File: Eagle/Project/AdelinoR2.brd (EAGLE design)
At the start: 47 x 53.3 mm, 79 parts, among them J1 DC-044-A, J2 YELLOW-8P-2.54, J3 YELLOW-6P-2.54, J4 YELLOW-8P-2.54, J5 YELLOW-8P-2.54, J6 4P-2.0, J7 YELLOW-2X3P-2.54, J8 4P-2.0, Q1 NCE3407A, Q2 CJ2305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

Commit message: Routing wip.
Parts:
- removed D1, D2: 1K 1/10W, Seeed-Fuse:D0603
- added ESD1: PRTR5V0U2X, Seeed-OPL-2017-01-Diode-james:SOT-143B
- moved Q2 17.5 mm to (7.49, 26.7), turned to 90 degrees
- moved R8 14.4 mm to (7.49, 28.8), turned to 270 degrees
- moved F1 8.42 mm to (8.51, 39.0), turned to 0 degrees
- moved R2 3.67 mm to (11.3, 36.4), turned to 0 degrees
- moved R3 3.64 mm to (11.3, 34.0), turned to 0 degrees
- moved D6 1.09 mm to (5.84, 22.2)
- moved L1 1.08 mm to (8.51, 34.0)
- moved C1 0.13 mm to (18.4, 26.7)
- moved C10 0.13 mm to (14.6, 26.7)
- moved C9 0.13 mm to (16.8, 26.7)
- moved R13 0.13 mm to (37.1, 24.9)
- moved R14 0.13 mm to (34.9, 24.9)
- moved R6 0.13 mm to (11.9, 27.6)
- moved X1 0.13 mm to (33.0, 45.8)
- moved R7 0.13 mm to (11.9, 25.8)
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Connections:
- net GND: no longer D1.1, D2.1
- net N$1: now also ESD1.3; no longer D1.2
- net N$2: now also ESD1.2; no longer D2.2
- net N$9: now also ESD1.4
- net UGND: now also ESD1.1
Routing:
- net RESET: track 21.1 -> 110.1 mm
- net PIN_D13: track 2.95 -> 88.8 mm, vias 0 -> 3
- net ACT_LED: track 0.00 -> 43.7 mm, vias 0 -> 4
- net PIN_D11: track 3.07 -> 37.6 mm, vias 0 -> 2
- net PIN_D10: track 2.70 -> 32.9 mm, vias 0 -> 1
- net PIN_D12: track 2.70 -> 30.6 mm, vias 0 -> 1
- net PIN_D9: track 2.57 -> 29.1 mm, vias 0 -> 1
- net PIN_D8: track 2.45 -> 26.0 mm, vias 0 -> 1
- net VUSB: track 19.3 -> 41.0 mm, vias 0 -> 1
- net PIN_D5: track 2.82 -> 24.1 mm, vias 0 -> 1
- net PIN_D6: track 2.57 -> 21.0 mm, vias 0 -> 1
- net PIN_D4: track 2.82 -> 20.4 mm, vias 0 -> 1
- net +3V3: track 26.1 -> 43.2 mm
- net PIN_D3: track 63.7 -> 49.7 mm
- net N$9: track 17.7 -> 4.82 mm
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- added copper zone on layer 16, net +5V

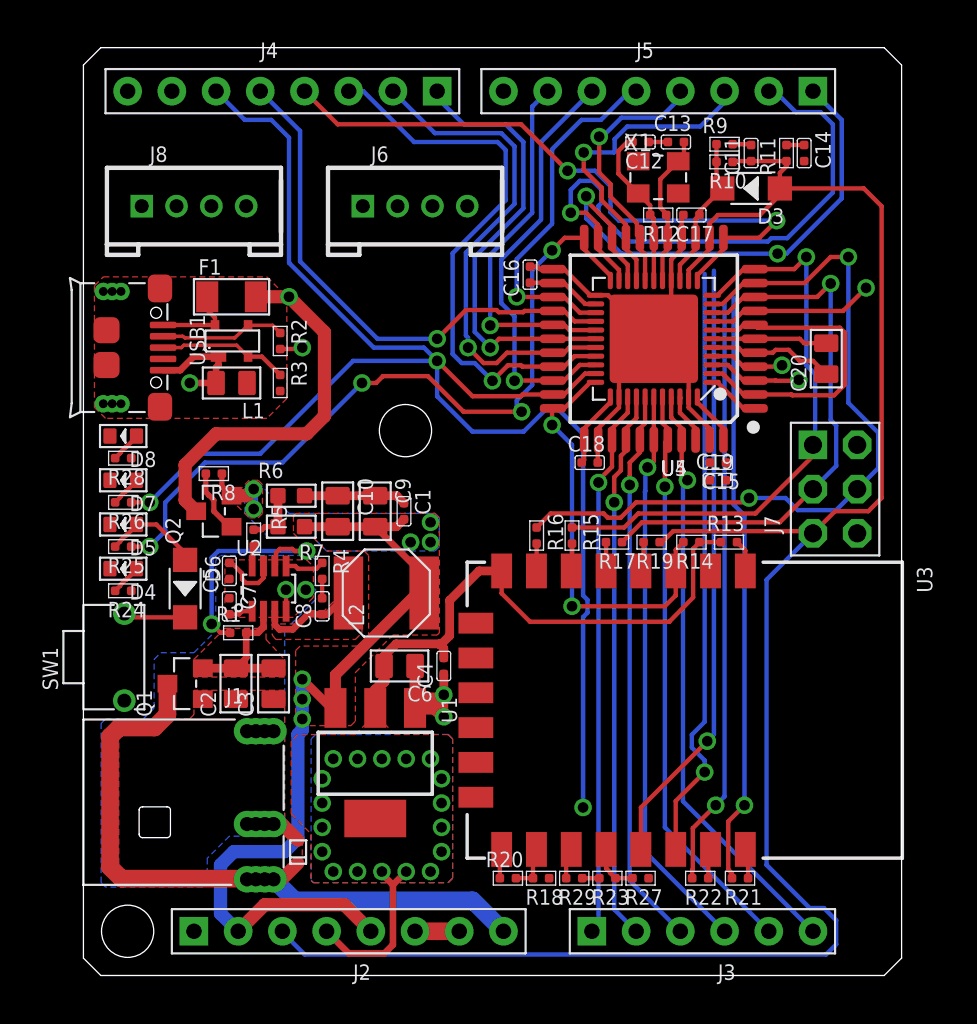
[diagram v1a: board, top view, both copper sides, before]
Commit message: Add ATECC608 crypto chip; routing wip.
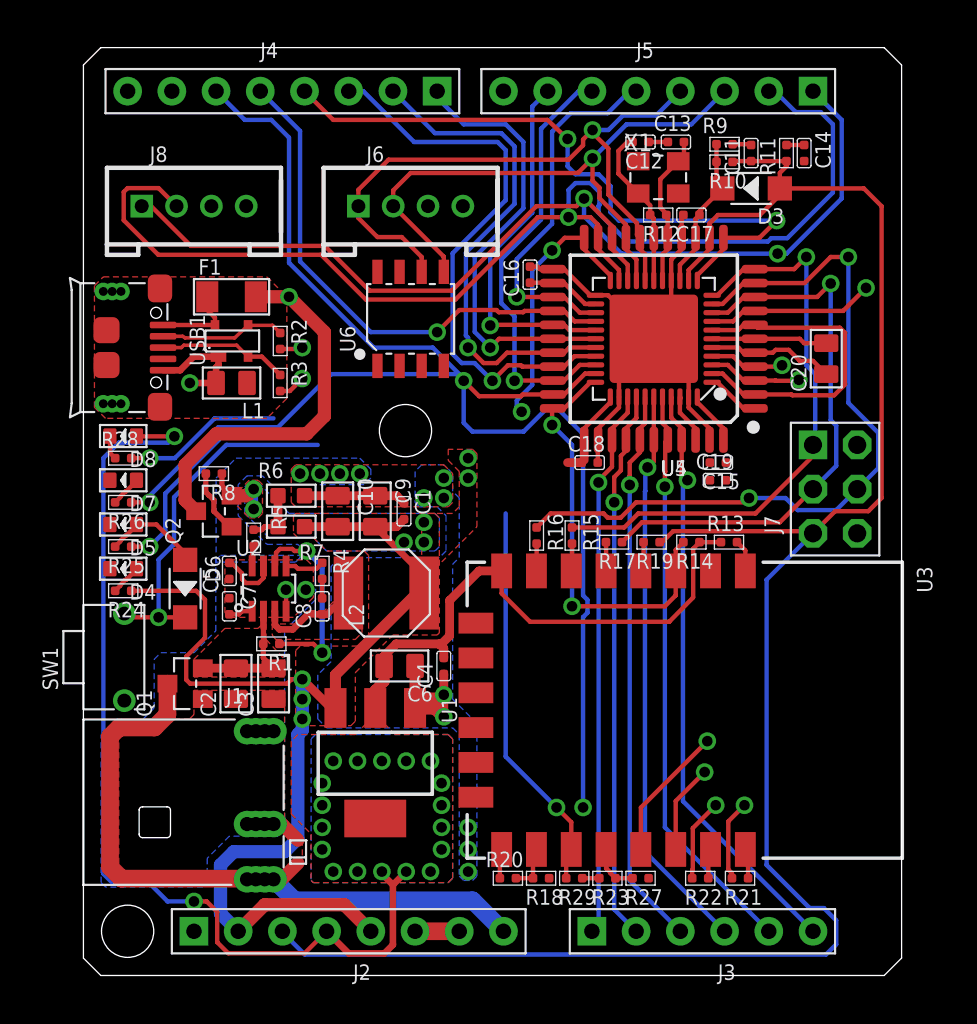
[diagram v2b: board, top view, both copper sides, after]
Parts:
- added U6: ATECC608-SOIC8, Adelino-Misc:SOIC8-1.27-5X4MM
- moved R1 2.01 mm to (10.8, 19.1), turned to 270 degrees
- moved J6 0.25 mm to (18.8, 44.2)
- turned R28 to 90 degrees
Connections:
- removed net PIN_D2: J5.3, J6.2, U3.19, U4.19, U5.19
- removed net PIN_D3: J5.4, J6.1, U3.20, U4.18, U5.18
- removed net _ESP: D8.+, R28.2
- new net N$4: D8.-, R28.1
- new net PIN_D2_SDA: J5.3, J6.2, U3.19, U4.19, U5.19, U6.5
- new net PIN_D3_SCL: J5.4, J6.1, U3.20, U4.18, U5.18, U6.6
- net +3V3: now also D8.+; no longer R28.1
- net +5V: now also U6.8
- net GND: now also U6.4
- net GPIO2_LED: now also R28.2; no longer D8.-
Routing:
- net PIN_D2: track 53.9 -> 0.00 mm, vias 2 -> 0
- net PIN_D3: track 49.7 -> 0.00 mm, vias 2 -> 0
- net +3V3: track 43.2 -> 90.1 mm, vias 18 -> 20
- net PIN_D2_SDA: track 0.00 -> 43.1 mm, vias 0 -> 2
- net PIN_D3_SCL: track 0.00 -> 43.1 mm, vias 0 -> 2
- net GPIO2_LED: track 1.77 -> 31.8 mm, vias 0 -> 2
- net +5V: track 74.9 -> 92.1 mm, vias 8 -> 10
- net RSTAT: track 4.66 -> 21.4 mm, vias 0 -> 1
- net ACT_LED: track 43.7 -> 29.2 mm, vias 4 -> 3
- net PIN_D1: track 68.0 -> 73.5 mm
- net SW_EN: track 13.4 -> 11.6 mm
- net _ESP: track 1.80 -> 0.00 mm
- net D+: track 4.30 -> 5.86 mm, vias 1 -> 2
- net N$4: track 0.00 -> 1.39 mm
- net PIN_D11: track 37.6 -> 38.5 mm
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
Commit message: Routing wip.
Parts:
- moved R27 2.16 mm to (29.8, 5.59), turned to 90 degrees
- moved R3 1.94 mm to (11.7, 35.9), turned to 90 degrees
- moved R23 1.65 mm to (31.8, 5.59), turned to 90 degrees
- moved R10 0.64 mm to (37.5, 46.7)
- moved R9 0.64 mm to (37.5, 47.8)
- moved R18 0.64 mm to (25.7, 5.59)
- moved R20 0.64 mm to (23.7, 5.59)
- moved R2 0.64 mm to (11.7, 37.0), turned to 90 degrees
- moved C11 0.63 mm to (39.0, 47.2)
- moved C14 0.63 mm to (42.0, 47.2)
- moved D3 0.63 mm to (39.0, 45.2)
- moved R11 0.63 mm to (41.0, 47.2)
- moved C20 0.52 mm to (42.8, 35.9)
- moved R15 0.38 mm to (28.1, 24.9), turned to 270 degrees
- moved R16 0.38 mm to (26.0, 24.9), turned to 270 degrees
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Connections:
- net +3V3: now also R28.1; no longer D8.+
- net GPIO2_LED: now also D8.-; no longer R28.2
- net N$4: now also D8.+, R28.2; no longer D8.-, R28.1
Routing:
- net +5V: track 92.1 -> 219.5 mm, vias 10 -> 13
- net PIN_D1: track 73.5 -> 140.7 mm, vias 2 -> 4
- net PIN_D0: track 64.9 -> 126.3 mm, vias 3 -> 4
- net RSTAT: track 21.4 -> 81.4 mm, vias 1 -> 2
- net AT_SS: track 9.64 -> 64.0 mm, vias 1 -> 3
- net UGND: track 13.9 -> 54.6 mm, vias 1 -> 2
- net D+: track 5.86 -> 42.2 mm
- net PIN_D3_SCL: track 43.1 -> 78.0 mm, vias 2 -> 3
- net PIN_D7: track 3.07 -> 37.7 mm, vias 0 -> 2
- net D-: track 6.68 -> 41.0 mm
- net PIN_D2_SDA: track 43.1 -> 73.1 mm, vias 2 -> 3
- net VUSB: track 41.0 -> 70.8 mm, vias 1 -> 3
- net +3V3: track 90.1 -> 109.9 mm
- net GPIO2_LED: track 31.8 -> 51.4 mm
- net ACT_LED: track 29.2 -> 45.2 mm, vias 3 -> 2
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
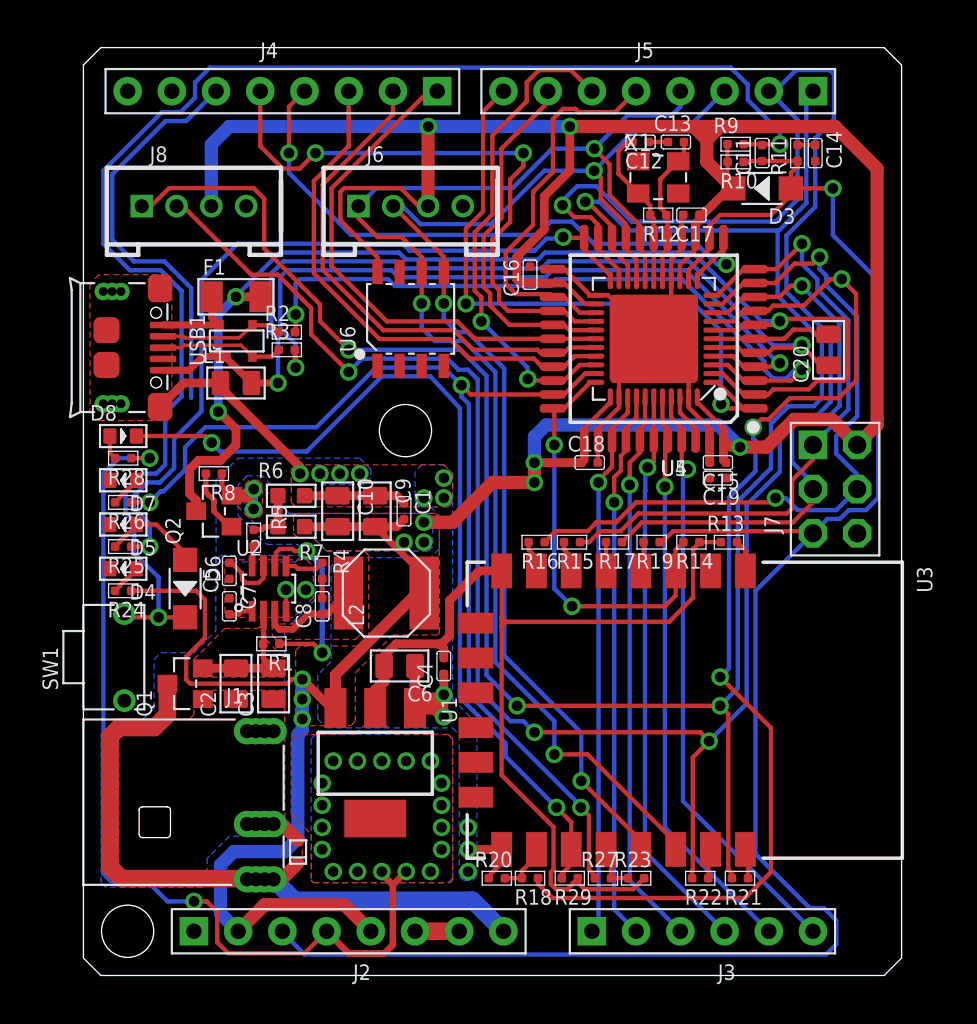
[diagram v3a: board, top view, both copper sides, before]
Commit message: Add decoupling cap for ECC608.
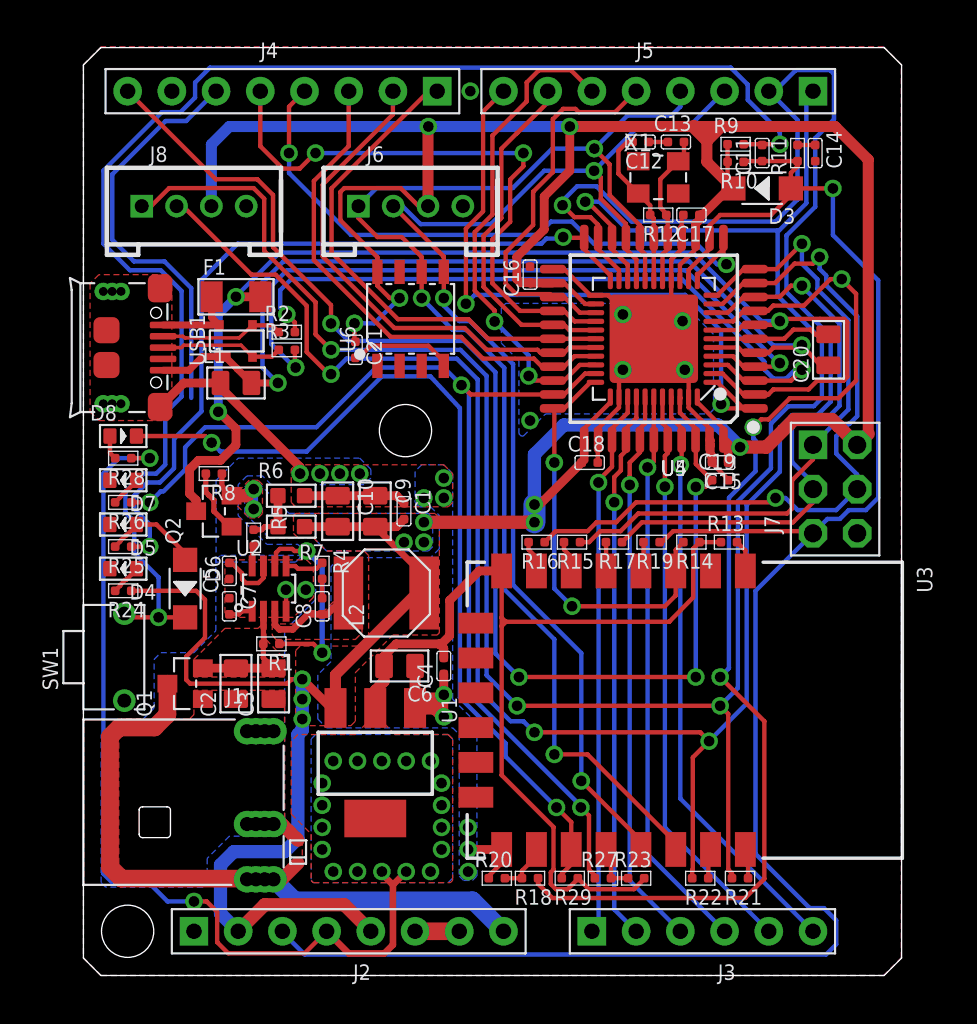
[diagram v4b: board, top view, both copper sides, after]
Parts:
- added C21: 100nf, Seeed-Capacitor:C0402
- moved C19 0.18 mm to (36.6, 28.4), turned to 90 degrees
- moved C15 0.13 mm to (36.6, 29.5)
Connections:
- removed net GND1: X1.P$2
- removed net GND2: X1.P$4
- net +5V: now also C21.1
- net GND: now also C21.2, X1.P$2, X1.P$4
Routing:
- net PIN_AREF: track 2.91 -> 76.0 mm, vias 0 -> 4
- net +5V: track 219.5 -> 227.5 mm, vias 13 -> 15
- net GND: track 73.9 -> 81.4 mm, vias 14 -> 20
- net PIN_D1: track 140.7 -> 141.4 mm
- net D-: track 41.0 -> 41.6 mm
- net AT_MISO: track 37.7 -> 37.0 mm
- net PIN_D0: track 126.3 -> 126.9 mm
- net PIN_D3_SCL: track 78.0 -> 77.4 mm

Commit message: Routing wip.
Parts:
- moved C18 0.13 mm to (29.0, 29.5)
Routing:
- net GND: track 81.4 -> 80.3 mm, vias 20 -> 22
- net +5V: track 227.5 -> 226.9 mm

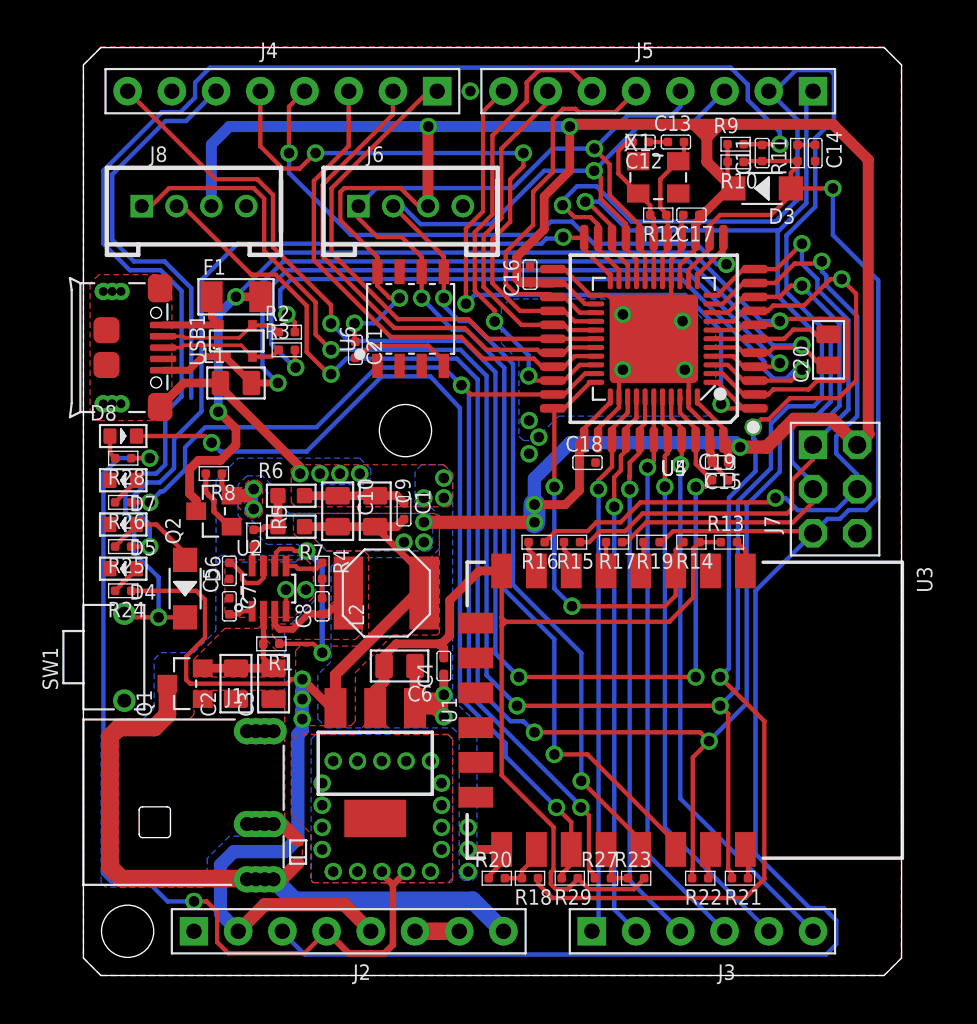
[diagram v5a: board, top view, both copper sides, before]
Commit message: Routing wip and DRC.
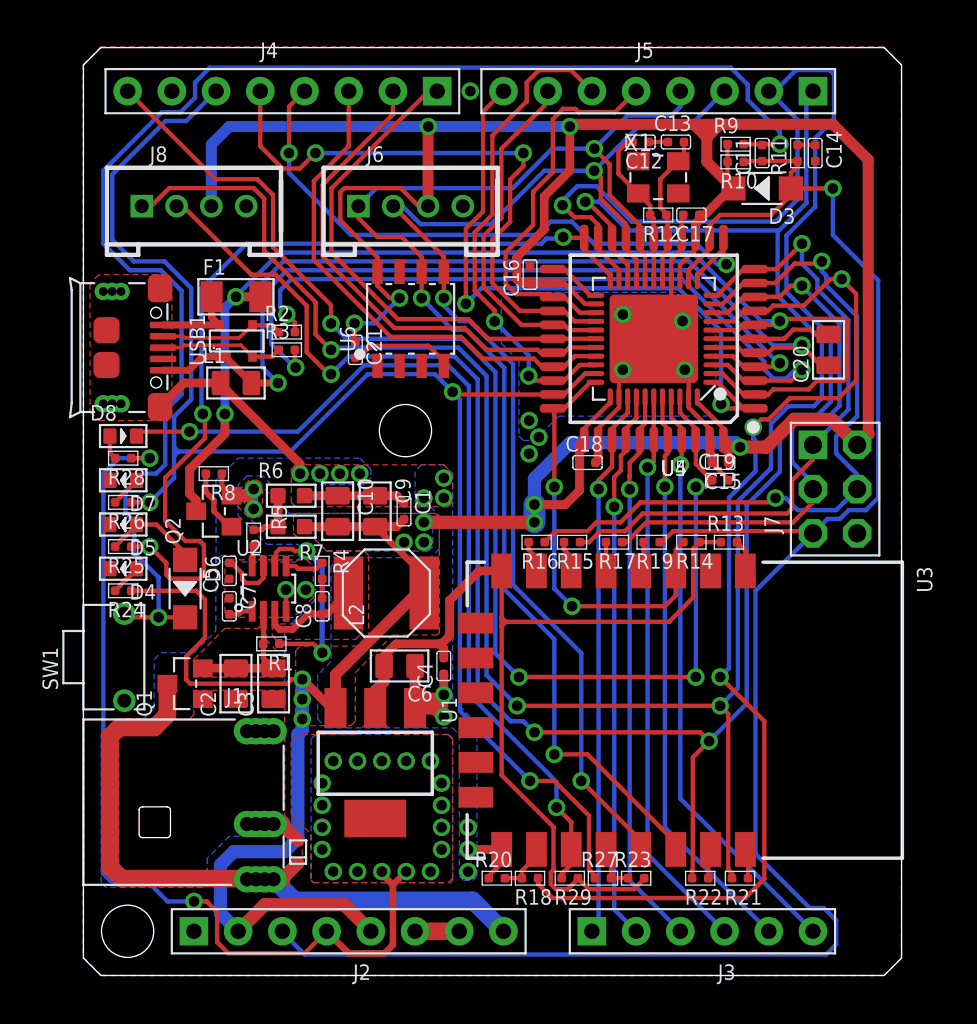
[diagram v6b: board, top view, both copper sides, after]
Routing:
- net ACT_LED: track 44.9 -> 50.6 mm, vias 2 -> 3
- net PIN_D13: track 87.0 -> 91.6 mm
- net GND: track 80.3 -> 82.4 mm
- net VIN: track 39.0 -> 41.0 mm
- net VUSB: track 70.5 -> 68.9 mm
- net GPIO2_LED: track 51.4 -> 52.2 mm
- net +5V: track 226.9 -> 226.4 mm

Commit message: Base X2 routing finished.
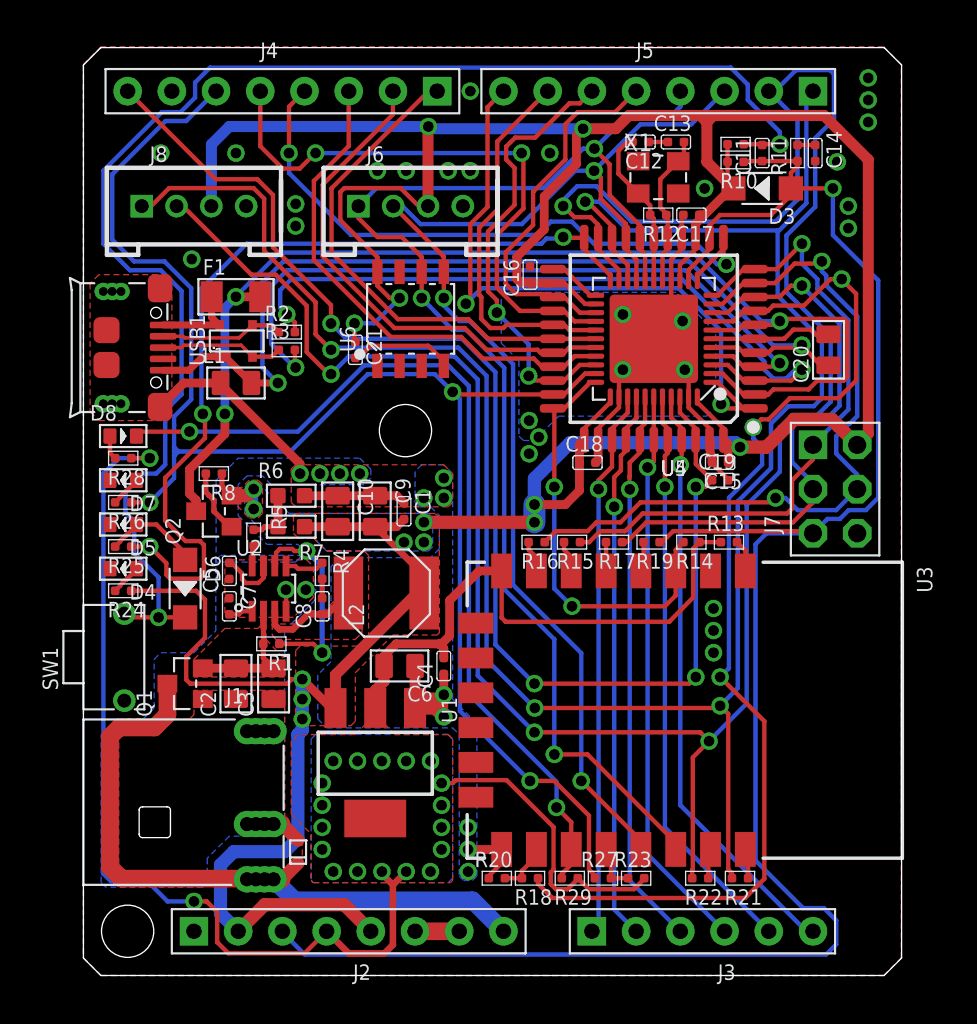
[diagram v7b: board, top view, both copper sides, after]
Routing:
- net +3V3: track 109.7 -> 103.7 mm
- net PIN_D5: track 28.2 -> 25.5 mm
- net RESET: track 109.3 -> 111.0 mm
- net PIN_D6: track 20.2 -> 21.7 mm
- net +5V: track 226.4 -> 227.3 mm
- net PIN_D4: track 22.0 -> 21.3 mm
- net GND: vias 22 -> 42

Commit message: Routing revision wip.
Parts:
- moved R10 0.25 mm to (37.5, 47.0)
- moved C11 0.25 mm to (39.0, 47.5)
- moved C14 0.25 mm to (42.0, 47.5)
- moved D3 0.25 mm to (39.0, 45.5)
- moved R11 0.25 mm to (41.0, 47.5)
- moved R9 0.25 mm to (37.5, 48.0)
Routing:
- net GND: track 82.4 -> 101.9 mm, vias 42 -> 53
- net PIN_AREF: track 76.0 -> 80.7 mm
- net PIN_A0: track 31.5 -> 35.8 mm
- net +5V: track 227.3 -> 223.2 mm
- net PIN_D0: track 126.6 -> 129.0 mm
- net PIN_D1: track 141.1 -> 143.4 mm
- net PIN_A1: track 31.7 -> 33.6 mm
- net RESET: track 111.0 -> 112.8 mm
- net AT_SS: track 64.0 -> 65.7 mm
- net +3V3: track 103.7 -> 102.0 mm
- net PIN_D4: track 21.3 -> 22.4 mm
- net ESP_EN: track 24.4 -> 23.5 mm
- net PIN_D3_SCL: track 77.4 -> 76.7 mm
- net PIN_A5: track 34.4 -> 34.9 mm
